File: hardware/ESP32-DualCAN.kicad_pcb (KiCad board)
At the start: 2 copper layers, 38.8 x 19.6 mm, 30 parts, among them J1 Molex 70553 6p, J2 Conn_01x10_Socket, J3 Conn_01x10_Socket, J4 holes, J5 pads, J6 holes, J7 pads, U1 LV2862Y, U3 TCAN1044AV, U4 TCAN1044AV, U5 ESP32-C6-Zero

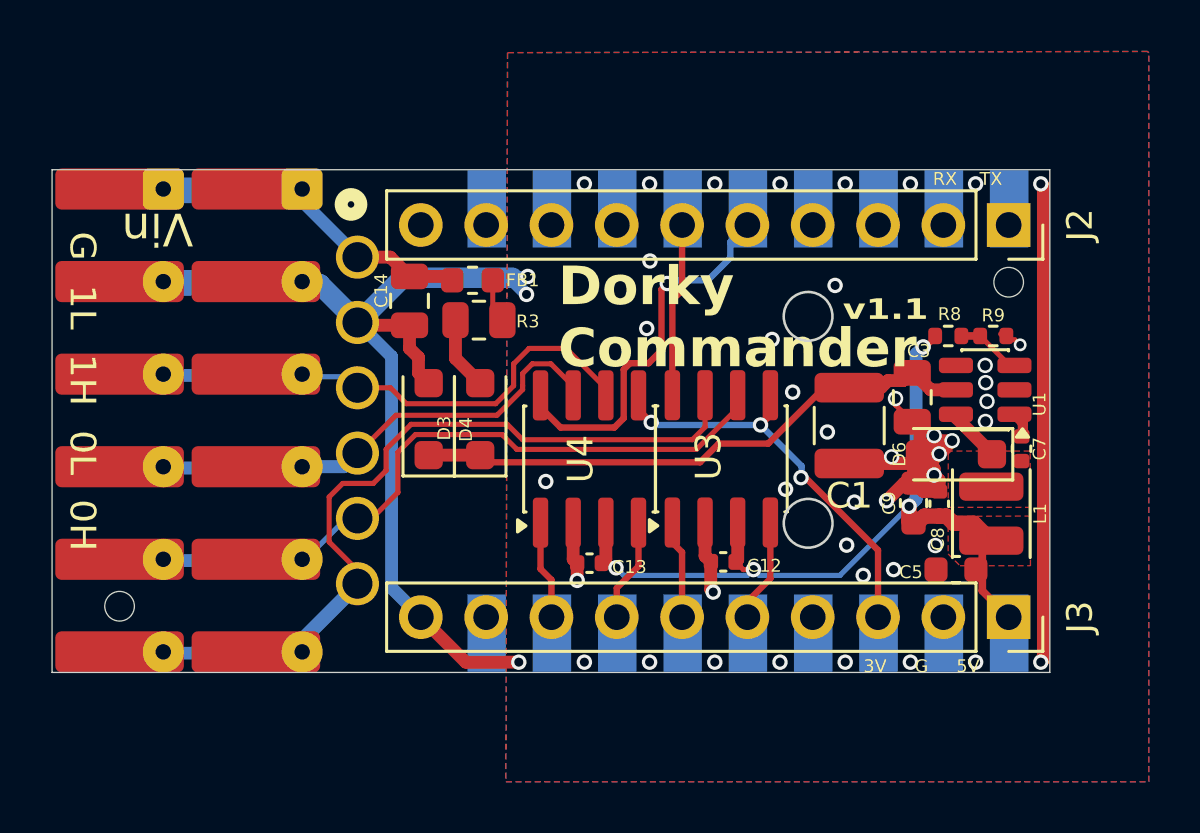
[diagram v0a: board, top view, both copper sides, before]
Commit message: Add power selector for can transceivers
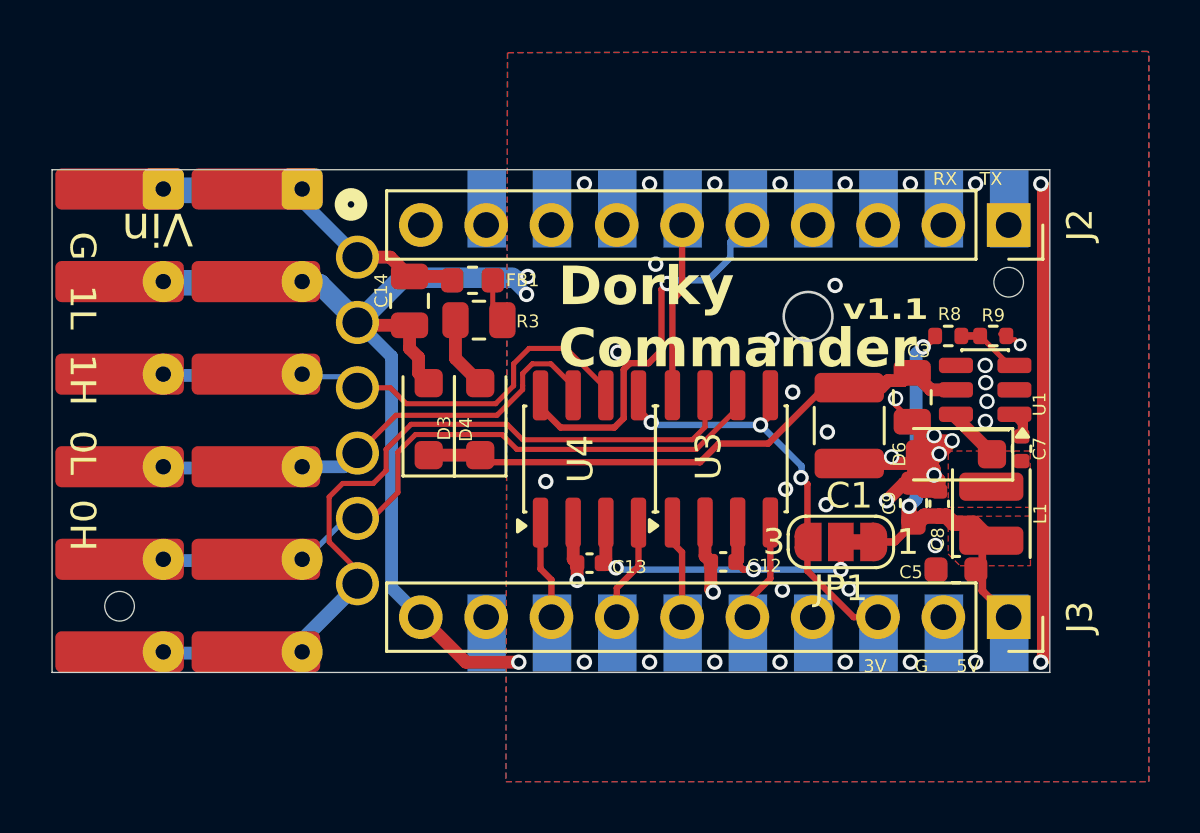
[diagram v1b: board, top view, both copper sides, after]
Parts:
- added JP1: SolderJumper_3_Bridged12, Jumper:SolderJumper-3_P1.3mm_Bridged12_RoundedPad1.0x1.5mm_NumberLabels, F.Cu at (152.3, 95.3)
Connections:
- C12 pad 1: +5V -> Net-(JP1-C)
- C13 pad 1: +5V -> Net-(JP1-C)
- U3 pad 3: +5V -> Net-(JP1-C)
- U4 pad 3: +5V -> Net-(JP1-C)
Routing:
- net Net-(JP1-C): track 0.00 -> 14.5 mm, vias 0 -> 3
- net +5V: track 34.1 -> 20.4 mm, vias 4 -> 2
- net +3.3V: track 16.3 -> 17.0 mm
- net GND: vias 46 -> 45
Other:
- outline, holes or cut-outs redrawn

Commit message: common 0603 100nF caps
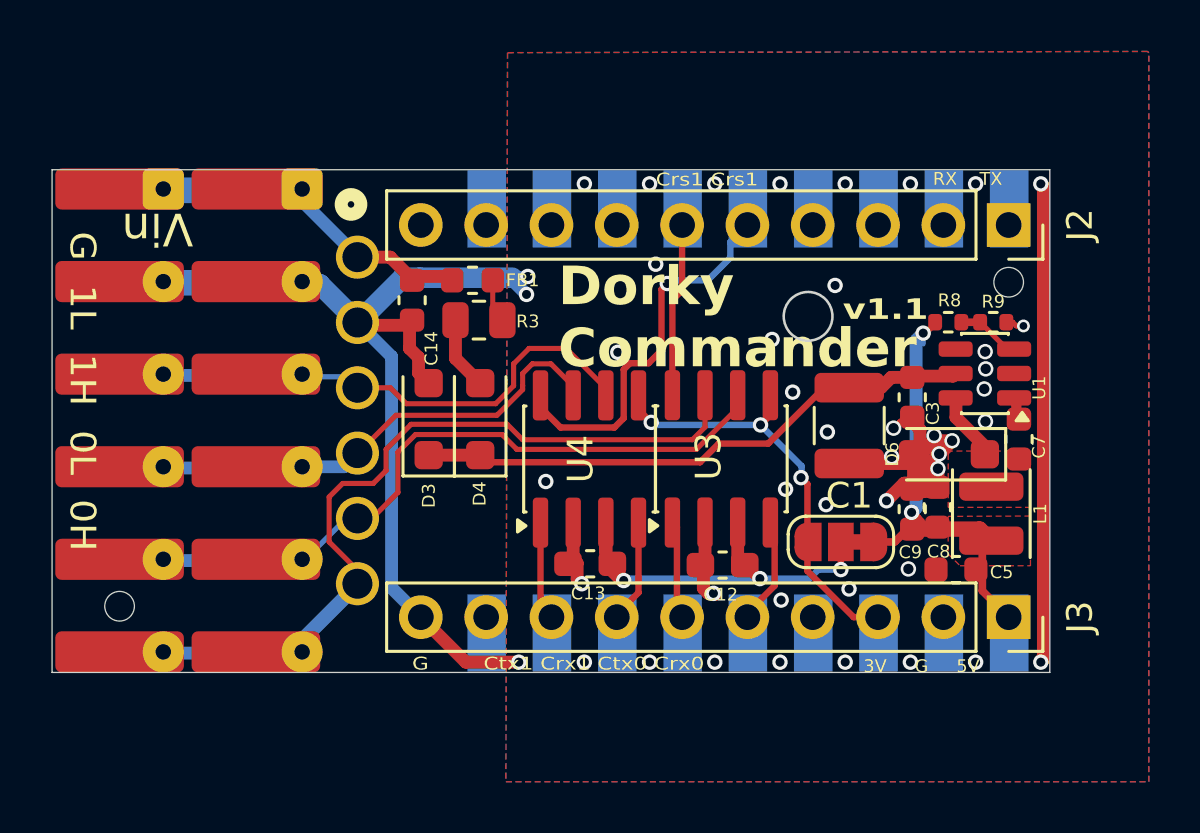
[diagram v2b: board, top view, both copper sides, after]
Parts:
- C12, C13: footprint Capacitor_SMD:C_0402_1005Metric -> Capacitor_SMD:C_0603_1608Metric_Pad1.08x0.95mm_HandSolder
- C14, C3: footprint Capacitor_SMD:C_0805_2012Metric -> Capacitor_SMD:C_0603_1608Metric
- C7, C8: footprint Capacitor_SMD:C_0402_1005Metric -> Capacitor_SMD:C_0603_1608Metric
- moved U1 0.64 mm to (157.9, 88.8)
- moved R8 0.53 mm to (156.5, 86.8)
- moved R9 0.53 mm to (158.2, 86.8)
- moved C7 0.39 mm to (159.2, 91.3)
- moved D6 0.28 mm to (156.5, 91.9)
- moved C9 0.24 mm to (155.1, 94.0)
- moved C8 0.15 mm to (156.1, 94.0)
- moved C12 0.13 mm to (147.7, 96.2)
- moved C14 0.10 mm to (135.7, 85.9)
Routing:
- net GND: track 82.0 -> 84.6 mm
- net Net-(JP1-C): track 14.5 -> 16.6 mm
- net Net-(D6-K): track 2.14 -> 3.01 mm
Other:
- board text added: "Crs1 Crs1"
- board text added: "G Ctx1 Crx1 Ctx0 Crx0"

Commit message: Vbat solder bridge for ESP32-C6-Zero-B
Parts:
- added D5: SMF30CA, Diode_SMD:D_SOD-123F, B.Cu at (135.6, 86.6)
- added JP2: SolderJumper_2_Open, Jumper:SolderJumper-2_P1.3mm_Open_TrianglePad1.0x1.5mm, F.Cu at (153.6, 85.7)
- D4: value SMF58CA -> SMF58A
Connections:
- net +5V renamed VCC
- D3 pad 2: unconnected-(D3-A-Pad2) -> Net-(D3-A)
- R3 pad 2: unconnected-(D3-A-Pad2) -> Net-(D3-A)
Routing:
- net +BATT: track 13.1 -> 40.5 mm
- net GND: track 84.6 -> 80.9 mm, vias 45 -> 44
- net unconnected-(D3-A-Pad2): track 2.94 -> 0.00 mm
- net Net-(D3-A): track 0.00 -> 2.94 mm
- net VCC: track 20.7 -> 22.9 mm
- net CAN0_RXD: vias 0 -> 1
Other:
- outline, holes or cut-outs redrawn
- board text added: "G _tx1 _rx1 _tx0 _rx0"
- board text added: "_rs1 _rs1"
- board text removed: "Crs1 Crs1"
- board text removed: "G Ctx1 Crx1 Ctx0 Crx0"
